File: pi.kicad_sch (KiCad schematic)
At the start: 4 parts, among them J1 Conn_02x20_Odd_Even, M1 Fan_4pin

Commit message: added gerbers and bom
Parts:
- added JP1: SolderJumper_3_Open, Jumper:SolderJumper-3_P1.3mm_Open_RoundedPad1.0x1.5mm, symbol Jumper:SolderJumper_3_Open
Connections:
- net +5V: now also JP1.1 (A); no longer M1.2 (+)
- new net: JP1.2 (C), M1.2 (+)
- new net +12V: JP1.3 (B)
- no-connect marks 0 -> 22
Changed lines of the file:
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@@
   (junction (at 163.195 69.85) (diameter 0) (color 0 0 0 0)
   )
+  (no_connect (at 147.955 115.57))
+  (no_connect (at 147.955 97.79))
+  (no_connect (at 160.655 87.63))
+  (no_connect (at 147.955 107.95))
+  (no_connect (at 160.655 95.25))
+  (no_connect (at 160.655 97.79))
+  (no_connect (at 147.955 95.25))
+  (no_connect (at 160.655 107.95))
+  (no_connect (at 160.655 113.03))
+  (no_connect (at 147.955 110.49))
+  (no_connect (at 147.955 105.41))
+  (no_connect (at 147.955 90.17))
+  (no_connect (at 147.955 72.39))
+  (no_connect (at 160.655 100.33))
+  (no_connect (at 147.955 102.87))
+  (no_connect (at 160.655 118.11))
+  (no_connect (at 160.655 115.57))
+  (no_connect (at 147.955 92.71))
+  (no_connect (at 147.955 77.47))
+  (no_connect (at 147.955 113.03))
+  (no_connect (at 147.955 74.93))
+  (no_connect (at 160.655 102.87))
   (wire (pts (xy 160.655 69.85) (xy 163.195 69.85))
     (stroke (width 0) (type default))
@@
     (stroke (width 0) (type default))
   )
+  (wire (pts (xy 104.775 106.68) (xy 104.775 108.585))
+    (stroke (width 0) (type default))
+  )
   (wire (pts (xy 90.805 123.825) (xy 102.235 123.825))
     (stroke (width 0) (type default))
   )
-  (wire (pts (xy 88.265 69.85) (xy 94.615 69.85))
-    (stroke (width 0) (type default))
-  )
   (wire (pts (xy 160.655 72.39) (xy 163.195 72.39))
     (stroke (width 0) (type default))
@@
   )
   (wire (pts (xy 140.97 68.58) (xy 140.97 72.39))
+    (stroke (width 0) (type default))
+  )
+  (wire (pts (xy 114.935 106.68) (xy 114.935 108.585))
     (stroke (width 0) (type default))
   )
@@
     (effects (font (size 1.27 1.27)) (justify right))
   )
-  (hierarchical_label "+3V3" (shape output) (at 88.265 69.85 180) (fields_autoplaced)
-    (effects (font (size 1.27 1.27)) (justify right))
-  )
   (hierarchical_label "BUCK_POWER_GOOD" (shape input) (at 88.265 74.93 180) (fields_autoplaced)
     (effects (font (size 1.27 1.27)) (justify right))
@@
     )
   )
+  (symbol (lib_id "power:+12V") (at 114.935 106.68 0) (unit 1)
+    (in_bom yes) (on_board yes) (dnp no) (fields_autoplaced)
+    (property "Reference" "#PWR091" (at 114.935 110.49 0)
+      (effects (font (size 1.27 1.27)) hide)
+    )
+    (property "Value" "+12V" (at 114.935 101.6 0)
+      (effects (font (size 1.27 1.27)))
+    )
+    (property "Footprint" "" (at 114.935 106.68 0)
+      (effects (font (size 1.27 1.27)) hide)
+    )
+    (property "Datasheet" "" (at 114.935 106.68 0)
+      (effects (font (size 1.27 1.27)) hide)
+    )
+    (pin "1")
+    (instances
+      (project "bitaxeUltra"
+        (path "/e63e39d7-6ac0-4ffd-8aa3-1841a4541b55/9bc1a7d6-07fa-4858-9423-fb2dbf7da294"
+          (reference "#PWR091") (unit 1)
+        )
+      )
+    )
+  )
   (symbol (lib_id "pearldiver-rescue:GND-pearldiver-rescue") (at 160.655 105.41 90) (unit 1)
     (in_bom yes) (on_board yes) (dnp no)
@@
         (path "/e63e39d7-6ac0-4ffd-8aa3-1841a4541b55/9bc1a7d6-07fa-4858-9423-fb2dbf7da294"
           (reference "#PWR064") (unit 1)
+        )
+      )
+    )
+  )
+  (symbol (lib_id "Jumper:SolderJumper_3_Open") (at 109.855 108.585 0) (unit 1)
+    (in_bom yes) (on_board yes) (dnp no) (fields_autoplaced)
+    (property "Reference" "JP1" (at 109.855 105.41 0)
+      (effects (font (size 1.27 1.27)))
+    )
+    (property "Value" "SolderJumper_3_Open" (at 109.855 105.41 0)
+      (effects (font (size 1.27 1.27)) hide)
+    )
+    (property "Footprint" "Jumper:SolderJumper-3_P1.3mm_Open_RoundedPad1.0x1.5mm" (at 109.855 108.585 0)
+      (effects (font (size 1.27 1.27)) hide)
+    )
+    (property "Datasheet" "~" (at 109.855 108.585 0)
+      (effects (font (size 1.27 1.27)) hide)
+    )
+    (pin "1")
+    (pin "2")
+    (pin "3")
+    (instances
+      (project "bitaxeUltra"
+        (path "/e63e39d7-6ac0-4ffd-8aa3-1841a4541b55/9bc1a7d6-07fa-4858-9423-fb2dbf7da294"
+          (reference "JP1") (unit 1)
         )
       )
@@
     )
   )
-  (symbol (lib_id "power:+5V") (at 109.855 112.395 0) (unit 1)
-    (in_bom yes) (on_board yes) (dnp no) (fields_autoplaced)
-    (property "Reference" "#PWR014" (at 109.855 116.205 0)
-      (effects (font (size 1.27 1.27)) hide)
-    )
-    (property "Value" "+5V" (at 109.855 107.95 0)
-      (effects (font (size 1.27 1.27)))
-    )
-    (property "Footprint" "" (at 109.855 112.395 0)
-      (effects (font (size 1.27 1.27)) hide)
-    )
-    (property "Datasheet" "" (at 109.855 112.395 0)
+  (symbol (lib_id "power:+5V") (at 104.775 106.68 0) (unit 1)
+    (in_bom yes) (on_board yes) (dnp no) (fields_autoplaced)
+    (property "Reference" "#PWR014" (at 104.775 110.49 0)
+      (effects (font (size 1.27 1.27)) hide)
+    )
+    (property "Value" "+5V" (at 104.775 102.235 0)
+      (effects (font (size 1.27 1.27)))
+    )
+    (property "Footprint" "" (at 104.775 106.68 0)
+      (effects (font (size 1.27 1.27)) hide)
+    )
+    (property "Datasheet" "" (at 104.775 106.68 0)
       (effects (font (size 1.27 1.27)) hide)
     )
@@
         )
       )
-    )
-  )
-  (symbol (lib_id "power:+3V3") (at 94.615 69.85 270) (unit 1)
-    (in_bom yes) (on_board yes) (dnp no) (fields_autoplaced)
-    (property "Reference" "#PWR021" (at 90.805 69.85 0)
-      (effects (font (size 1.27 1.27)) hide)
-    )
-    (property "Value" "+3V3" (at 97.79 69.85 90)
-      (effects (font (size 1.27 1.27)) (justify left))
-    )
-    (property "Footprint" "" (at 94.615 69.85 0)
-      (effects (font (size 1.27 1.27)) hide)
-    )
-    (property "Datasheet" "" (at 94.615 69.85 0)
-      (effects (font (size 1.27 1.27)) hide)
-    )
-    (pin "1")
-    (instances
-      (project "bitaxeUltra"
-        (path "/e63e39d7-6ac0-4ffd-8aa3-1841a4541b55/9bc1a7d6-07fa-4858-9423-fb2dbf7da294"
-          (reference "#PWR021") (unit 1)
-        )
-      )

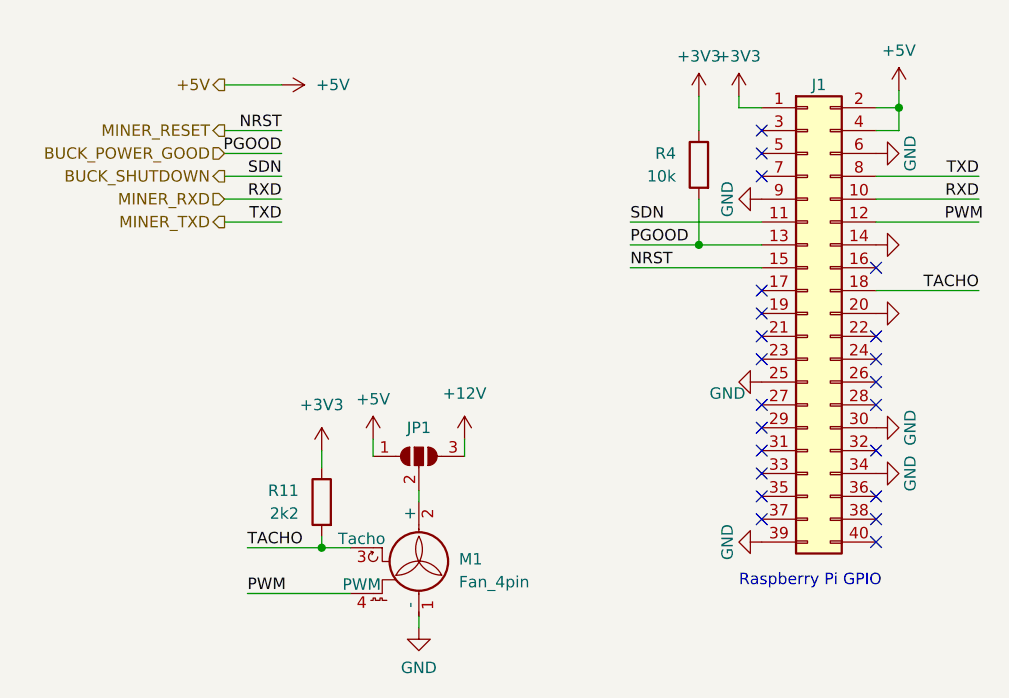
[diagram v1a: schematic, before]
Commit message: fixed some order numbers, added initial python code for testing
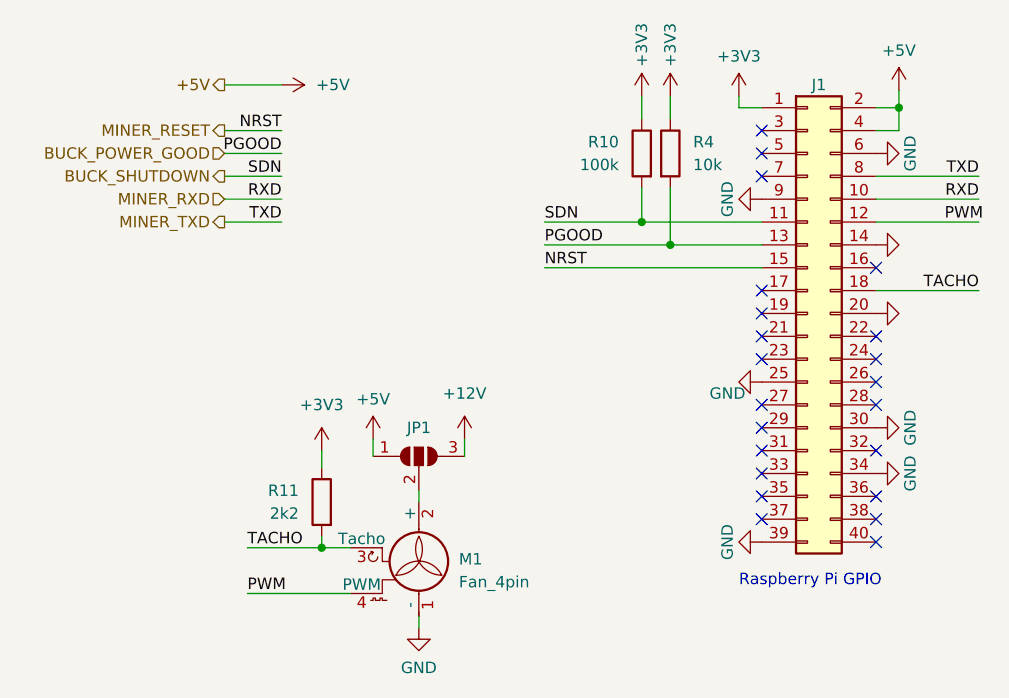
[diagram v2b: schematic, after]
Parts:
- added R10: 100k, Resistor_SMD:R_0805_2012Metric, symbol Device:R
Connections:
- net +3V3: now also R10.1
- net BUCK_SHUTDOWN: now also R10.2
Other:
- moved on the sheet: R4
